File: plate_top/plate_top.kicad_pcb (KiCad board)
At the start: 2 copper layers, 157.5 x 118.1 mm, 31 parts, among them SW1 SW_Push

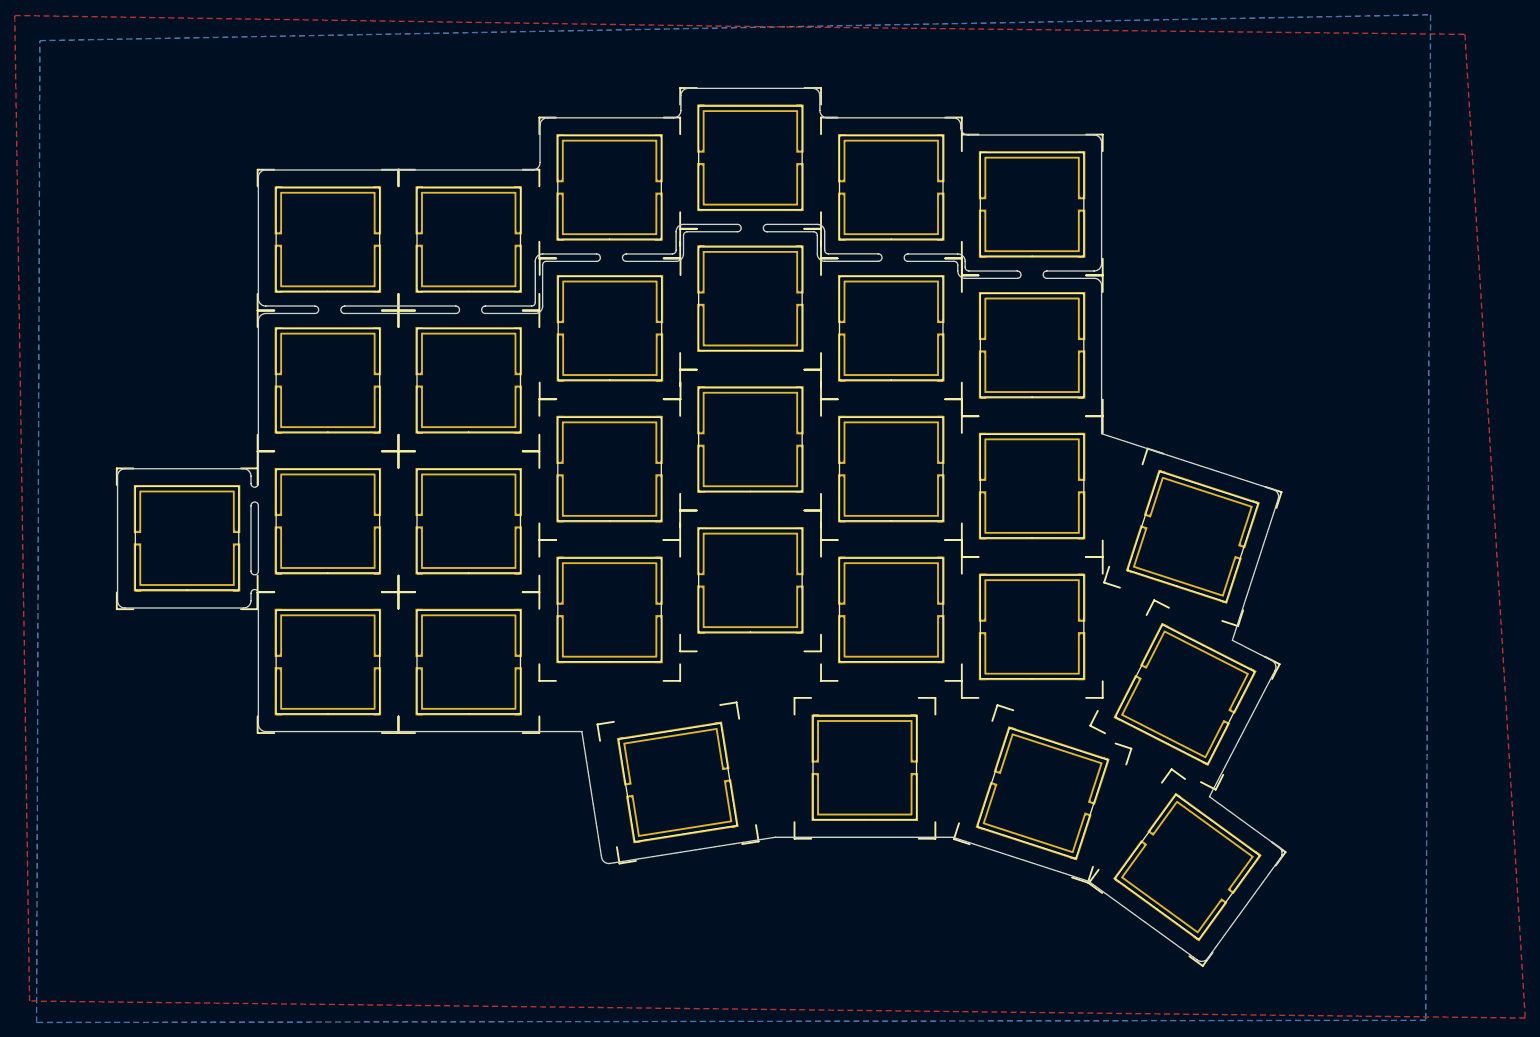
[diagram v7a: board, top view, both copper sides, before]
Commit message: Changed layer from silk to comments
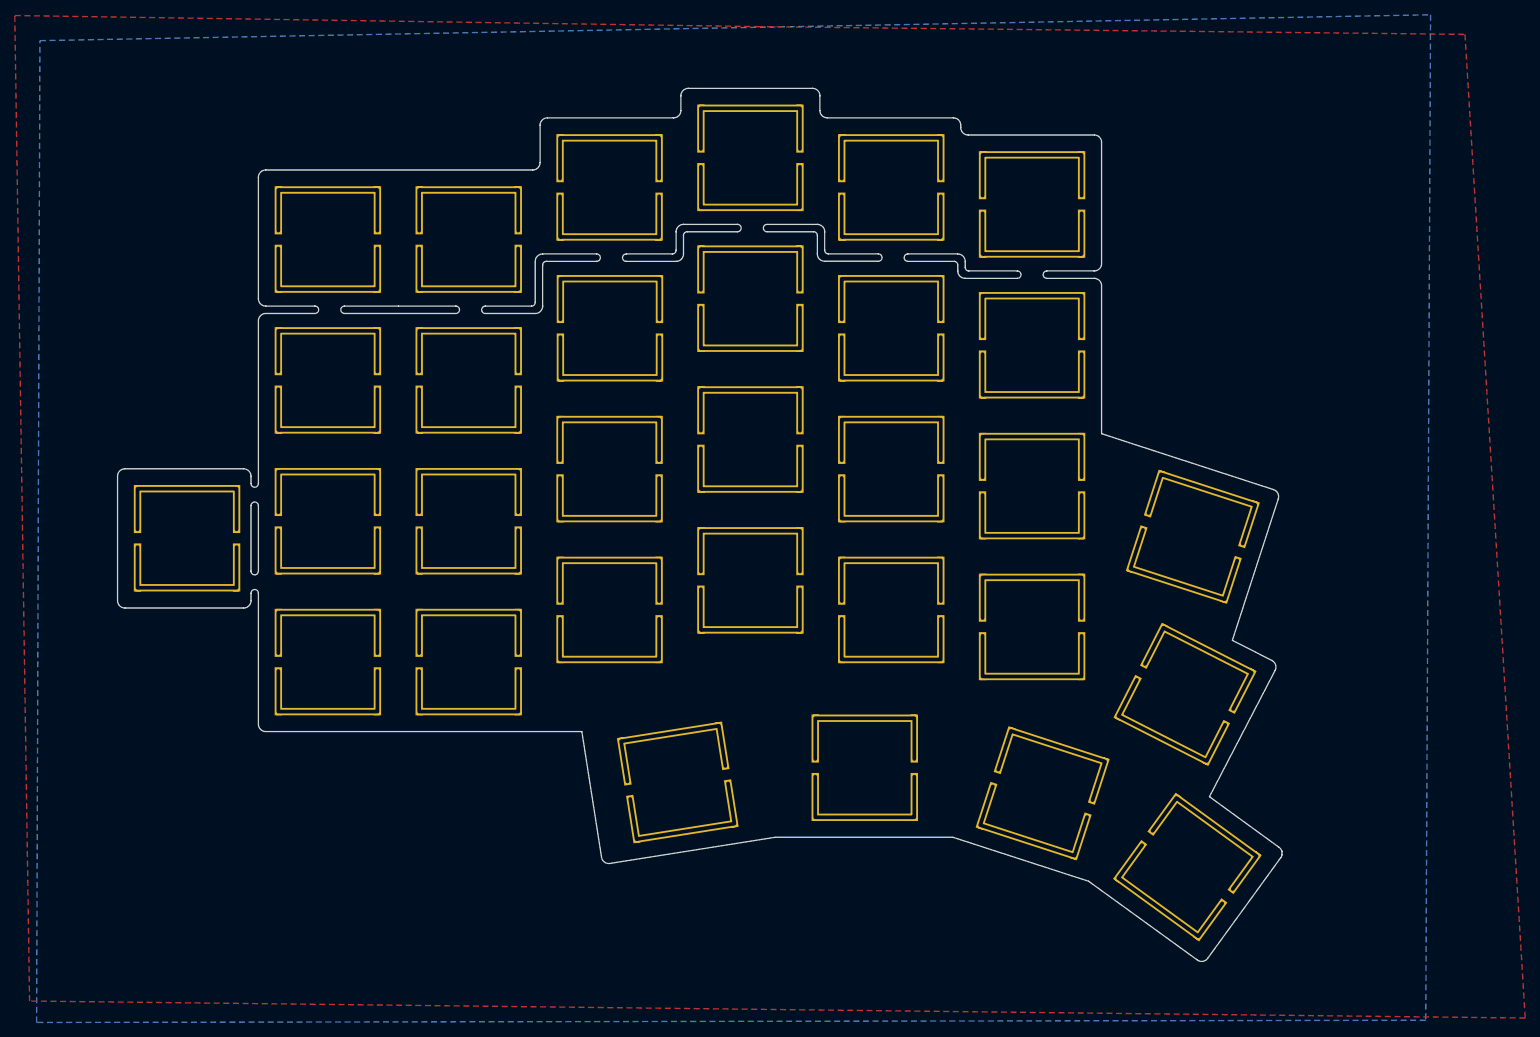
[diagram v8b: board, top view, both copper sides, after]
